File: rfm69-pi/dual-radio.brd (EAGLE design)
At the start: 100 x 80 mm, 7 parts, among them U1 RFM69HCW, U2 RFM69HCW, X1 BU-SMA-G, X2 RASPI_BOARD_B+#_HDC, X3 BU-SMA-G, X4 SMA-142-0701-871/876, X5 SMA-142-0701-871/876

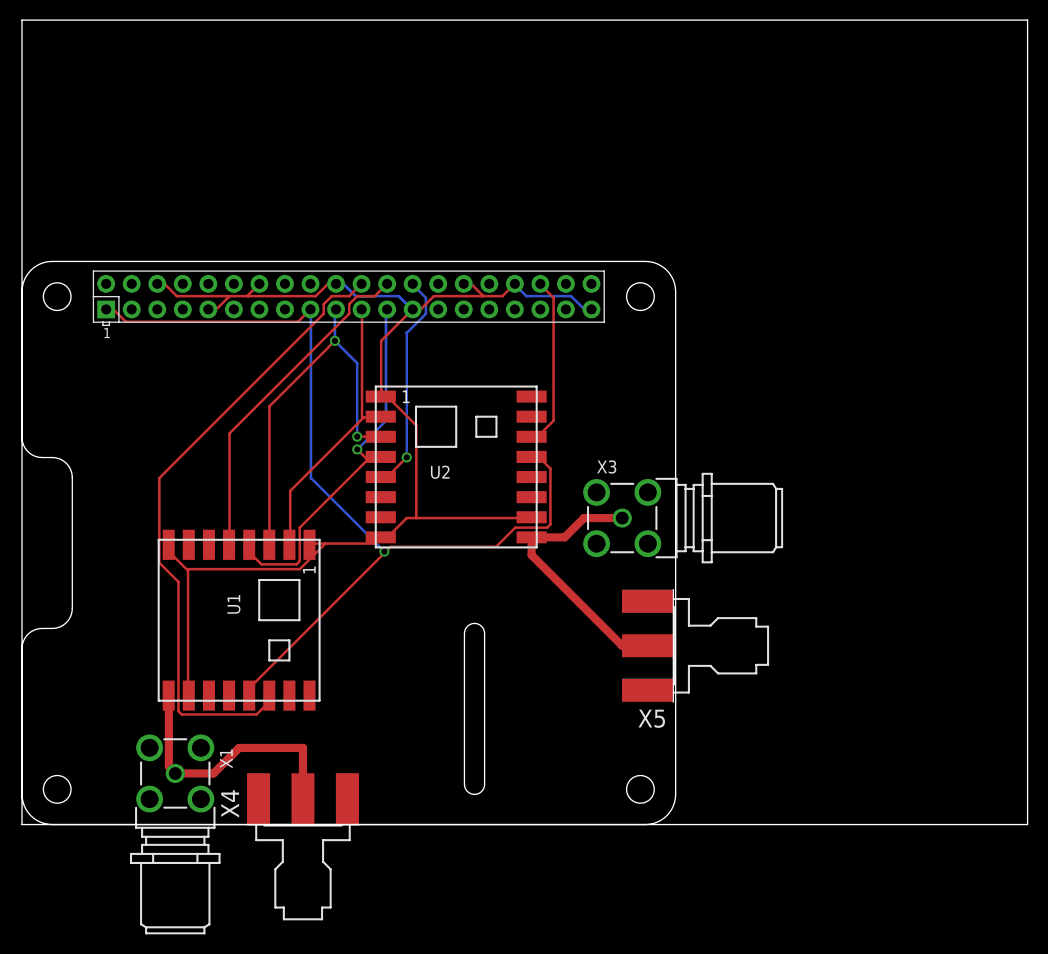
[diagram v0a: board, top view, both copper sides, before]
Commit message: Fix boards and add the pi control station
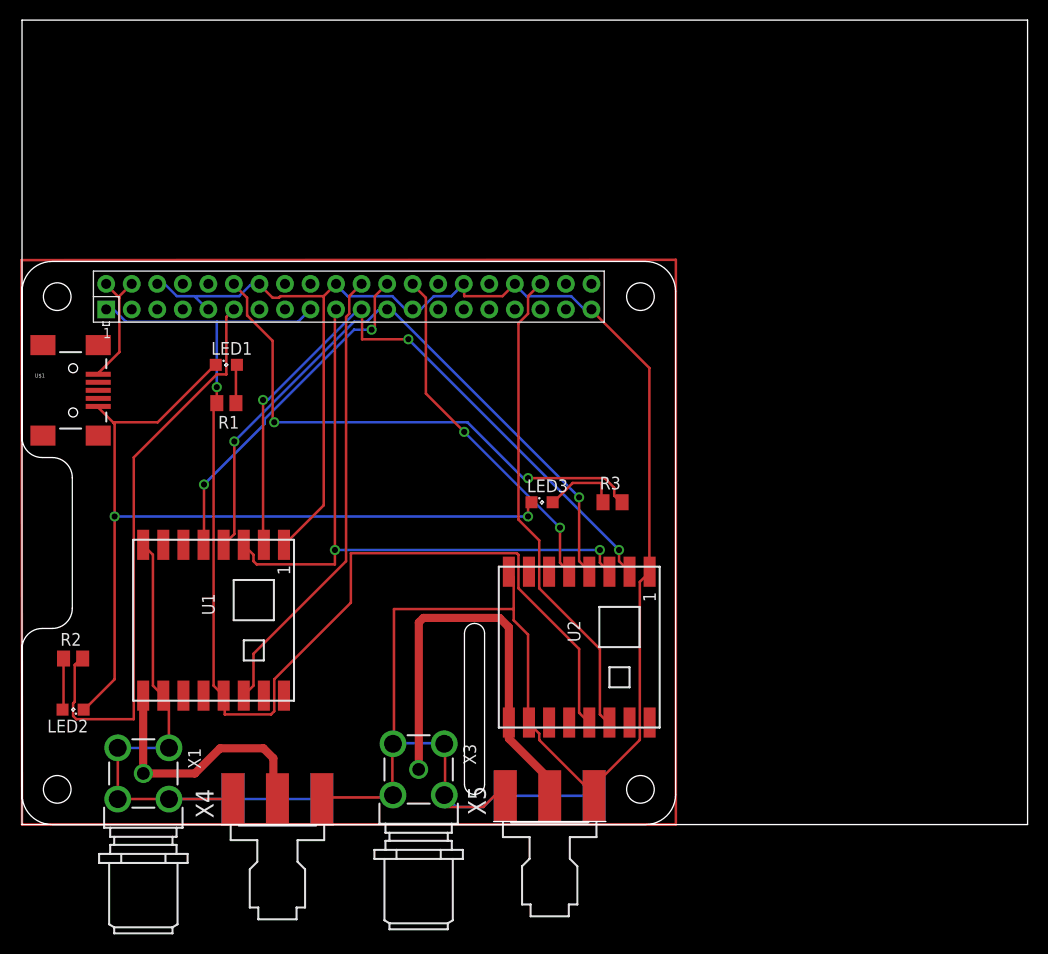
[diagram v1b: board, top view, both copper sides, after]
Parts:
- added LED1, LED2, LED3: (no value), led:SML0805
- added R1, R2, R3: 100, resistor:M0805
- added U$1: USB-MINIB-5PIN, SparkFun-Connectors:USB-MINIB
- moved X3 32.2 mm to (39.4, 5.48), turned to 270 degrees
- moved U2 21.7 mm to (55.4, 17.6), turned to 270 degrees
- moved X5 21.4 mm to (52.5, 0.30), turned to 90 degrees
- moved X1 3.18 mm to (12.1, 5.08)
- moved X4 2.54 mm to (25.4, 0.00)
- moved U1 2.54 mm to (19.1, 20.3)
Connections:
- removed net 5V0A: X2.2
- removed net 5V0B: X2.4
- new net GND: LED1.C, LED2.C, LED3.C, U$1.GND
- new net N$12: R2.2, X2.11
- new net N$13: R3.2, X2.12
- new net N$14: LED1.A, R1.1
- new net N$15: LED2.A, R2.1
- new net N$16: LED3.A, R3.1
- new net N$17: U$1.VBUS, X2.2, X2.4
- net N$1: now also R1.2
- net N$7: now also X1.2, X1.3, X1.4, X1.5, X3.2, X3.3, X3.4, X3.5, X4.G@1, X4.G@2, X4.G@3, X4.G@4, X5.G@1, X5.G@2, X5.G@3, X5.G@4
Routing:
- net N$18: track 0.00 -> 242.4 mm
- net N$7: track 132.2 -> 294.8 mm
- net GND: track 0.00 -> 87.3 mm, vias 0 -> 2
- net N$12: track 0.00 -> 57.8 mm
- net N$13: track 0.00 -> 53.8 mm, vias 0 -> 2
- net N$2: track 28.3 -> 67.8 mm, vias 0 -> 3
- net N$9: track 17.0 -> 48.4 mm
- net N$4: track 38.6 -> 66.0 mm, vias 1 -> 2
- net N$1: track 93.9 -> 121.3 mm
- net N$3: track 38.9 -> 64.6 mm
- net N$8: track 62.9 -> 45.8 mm
- net N$11: track 26.8 -> 42.8 mm
- net N$6: track 22.0 -> 35.1 mm, vias 1 -> 2
- net N$17: track 0.00 -> 12.3 mm
- net N$16: track 0.00 -> 7.70 mm
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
